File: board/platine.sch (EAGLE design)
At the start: 47 parts, among them IC2 SPS-1, T1 BC846, T2 BC846, X11 22-23-2031, X15 22-23-2031, X16 22-23-2031, X17 22-23-2031, X18 22-23-2031, X3 1751251, X4 1751251, X5 1751251, X7 1751248, X8 1751248, X9 1751248

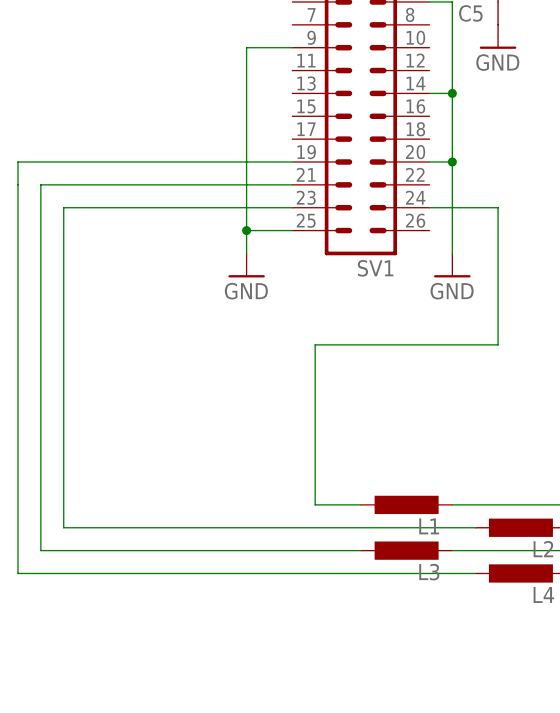
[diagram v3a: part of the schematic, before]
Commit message: fix(board): switch MISO and MOSI
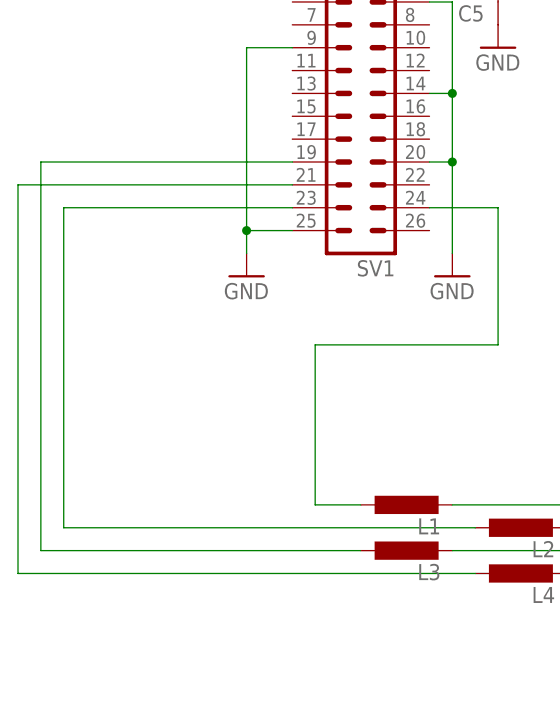
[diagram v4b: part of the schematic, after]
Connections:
- net N$46: now also SV1.19; no longer SV1.21
- net N$6: now also SV1.21; no longer SV1.19
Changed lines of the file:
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@@
 <?xml version="1.0" encoding="utf-8"?>
 <!DOCTYPE eagle SYSTEM "eagle.dtd">
-<eagle version="6.3">
+<eagle version="6.4">
 <drawing>
 <settings>
@@
 <grid distance="0.1" unitdist="inch" unit="inch" style="lines" multiple="1" display="no" altdistance="0.01" altunitdist="inch" altunit="inch"/>
 <layers>
-<layer number="1" name="Top" color="4" fill="1" visible="yes" active="no"/>
-<layer number="2" name="Route2" color="1" fill="3" visible="yes" active="no"/>
-<layer number="3" name="Route3" color="4" fill="3" visible="yes" active="no"/>
-<layer number="4" name="Route4" color="1" fill="4" visible="yes" active="no"/>
-<layer number="5" name="Route5" color="4" fill="4" visible="yes" active="no"/>
-<layer number="6" name="Route6" color="1" fill="8" visible="yes" active="no"/>
-<layer number="7" name="Route7" color="4" fill="8" visible="yes" active="no"/>
-<layer number="8" name="Route8" color="1" fill="2" visible="yes" active="no"/>
-<layer number="9" name="Route9" color="4" fill="2" visible="yes" active="no"/>
-<layer number="10" name="Route10" color="1" fill="7" visible="yes" active="no"/>
-<layer number="11" name="Route11" color="4" fill="7" visible="yes" active="no"/>
-<layer number="12" name="Route12" color="1" fill="5" visible="yes" active="no"/>
-<layer number="13" name="Route13" color="4" fill="5" visible="yes" active="no"/>
-<layer number="14" name="Route14" color="1" fill="6" visible="yes" active="no"/>
-<layer number="15" name="Route15" color="4" fill="6" visible="yes" active="no"/>
-<layer number="16" name="Bottom" color="1" fill="1" visible="yes" active="no"/>
-<layer number="17" name="Pads" color="2" fill="1" visible="yes" active="no"/>
-<layer number="18" name="Vias" color="2" fill="1" visible="yes" active="no"/>
-<layer number="19" name="Unrouted" color="6" fill="1" visible="yes" active="no"/>
-<layer number="20" name="Dimension" color="15" fill="1" visible="yes" active="no"/>
-<layer number="21" name="tPlace" color="7" fill="1" visible="yes" active="no"/>
-<layer number="22" name="bPlace" color="7" fill="1" visible="yes" active="no"/>
-<layer number="23" name="tOrigins" color="15" fill="1" visible="yes" active="no"/>
-<layer number="24" name="bOrigins" color="15" fill="1" visible="yes" active="no"/>
-<layer number="25" name="tNames" color="7" fill="1" visible="yes" active="no"/>
-<layer number="26" name="bNames" color="7" fill="1" visible="yes" active="no"/>
-<layer number="27" name="tValues" color="7" fill="1" visible="yes" active="no"/>
-<layer number="28" name="bValues" color="7" fill="1" visible="yes" active="no"/>
+<layer number="1" name="Top" color="4" fill="1" visible="no" active="no"/>
+<layer number="2" name="Route2" color="1" fill="3" visible="no" active="no"/>
+<layer number="3" name="Route3" color="4" fill="3" visible="no" active="no"/>
+<layer number="4" name="Route4" color="1" fill="4" visible="no" active="no"/>
+<layer number="5" name="Route5" color="4" fill="4" visible="no" active="no"/>
+<layer number="6" name="Route6" color="1" fill="8" visible="no" active="no"/>
+<layer number="7" name="Route7" color="4" fill="8" visible="no" active="no"/>
+<layer number="8" name="Route8" color="1" fill="2" visible="no" active="no"/>
+<layer number="9" name="Route9" color="4" fill="2" visible="no" active="no"/>
+<layer number="10" name="Route10" color="1" fill="7" visible="no" active="no"/>
+<layer number="11" name="Route11" color="4" fill="7" visible="no" active="no"/>
+<layer number="12" name="Route12" color="1" fill="5" visible="no" active="no"/>
+<layer number="13" name="Route13" color="4" fill="5" visible="no" active="no"/>
+<layer number="14" name="Route14" color="1" fill="6" visible="no" active="no"/>
+<layer number="15" name="Route15" color="4" fill="6" visible="no" active="no"/>
+<layer number="16" name="Bottom" color="1" fill="1" visible="no" active="no"/>
+<layer number="17" name="Pads" color="2" fill="1" visible="no" active="no"/>
+<layer number="18" name="Vias" color="2" fill="1" visible="no" active="no"/>
+<layer number="19" name="Unrouted" color="6" fill="1" visible="no" active="no"/>
+<layer number="20" name="Dimension" color="15" fill="1" visible="no" active="no"/>
+<layer number="21" name="tPlace" color="7" fill="1" visible="no" active="no"/>
+<layer number="22" name="bPlace" color="7" fill="1" visible="no" active="no"/>
+<layer number="23" name="tOrigins" color="15" fill="1" visible="no" active="no"/>
+<layer number="24" name="bOrigins" color="15" fill="1" visible="no" active="no"/>
+<layer number="25" name="tNames" color="7" fill="1" visible="no" active="no"/>
+<layer number="26" name="bNames" color="7" fill="1" visible="no" active="no"/>
+<layer number="27" name="tValues" color="7" fill="1" visible="no" active="no"/>
+<layer number="28" name="bValues" color="7" fill="1" visible="no" active="no"/>
 <layer number="29" name="tStop" color="7" fill="3" visible="no" active="no"/>
 <layer number="30" name="bStop" color="7" fill="6" visible="no" active="no"/>
@@
 <layer number="35" name="tGlue" color="7" fill="4" visible="no" active="no"/>
 <layer number="36" name="bGlue" color="7" fill="5" visible="no" active="no"/>
-<layer number="37" name="tTest" color="7" fill="1" visible="yes" active="no"/>
-<layer number="38" name="bTest" color="7" fill="1" visible="yes" active="no"/>
+<layer number="37" name="tTest" color="7" fill="1" visible="no" active="no"/>
+<layer number="38" name="bTest" color="7" fill="1" visible="no" active="no"/>
 <layer number="39" name="tKeepout" color="4" fill="11" visible="no" active="no"/>
 <layer number="40" name="bKeepout" color="1" fill="11" visible="no" active="no"/>
@@
 <layer number="44" name="Drills" color="7" fill="1" visible="no" active="no"/>
 <layer number="45" name="Holes" color="7" fill="1" visible="no" active="no"/>
-<layer number="46" name="Milling" color="3" fill="1" visible="yes" active="no"/>
-<layer number="47" name="Measures" color="7" fill="1" visible="yes" active="no"/>
-<layer number="48" name="Document" color="7" fill="1" visible="yes" active="no"/>
-<layer number="49" name="Reference" color="7" fill="1" visible="yes" active="no"/>
-<layer number="51" name="tDocu" color="7" fill="1" visible="yes" active="no"/>
-<layer number="52" name="bDocu" color="7" fill="1" visible="yes" active="no"/>
+<layer number="46" name="Milling" color="3" fill="1" visible="no" active="no"/>
+<layer number="47" name="Measures" color="7" fill="1" visible="no" active="no"/>
+<layer number="48" name="Document" color="7" fill="1" visible="no" active="no"/>
+<layer number="49" name="Reference" color="7" fill="1" visible="no" active="no"/>
+<layer number="51" name="tDocu" color="7" fill="1" visible="no" active="no"/>
+<layer number="52" name="bDocu" color="7" fill="1" visible="no" active="no"/>
 <layer number="91" name="Nets" color="2" fill="1" visible="yes" active="yes"/>
 <layer number="92" name="Busses" color="1" fill="1" visible="yes" active="yes"/>
@@
 <pinref part="L4" gate="G$1" pin="1"/>
 <wire x1="-12.7" y1="68.58" x2="-63.5" y2="68.58" width="0.1524" layer="91"/>
-<pinref part="SV1" gate="G$1" pin="19"/>
-<wire x1="-33.02" y1="114.3" x2="-63.5" y2="114.3" width="0.1524" layer="91"/>
-<wire x1="-63.5" y1="114.3" x2="-63.5" y2="111.76" width="0.1524" layer="91"/>
+<pinref part="SV1" gate="G$1" pin="21"/>
+<wire x1="-63.5" y1="111.76" x2="-33.02" y2="111.76" width="0.1524" layer="91"/>
 </segment>
 </net>
@@
 <segment>
 <pinref part="L3" gate="G$1" pin="1"/>
-<wire x1="-60.96" y1="111.76" x2="-60.96" y2="71.12" width="0.1524" layer="91"/>
+<wire x1="-60.96" y1="114.3" x2="-60.96" y2="71.12" width="0.1524" layer="91"/>
 <wire x1="-25.4" y1="71.12" x2="-60.96" y2="71.12" width="0.1524" layer="91"/>
-<pinref part="SV1" gate="G$1" pin="21"/>
-<wire x1="-33.02" y1="111.76" x2="-60.96" y2="111.76" width="0.1524" layer="91"/>
-</segment>
-</net>
+<pinref part="SV1" gate="G$1" pin="19"/>
+<wire x1="-60.96" y1="114.3" x2="-33.02" y2="114.3" width="0.1524" layer="91"/>
+</segment>
+</net>

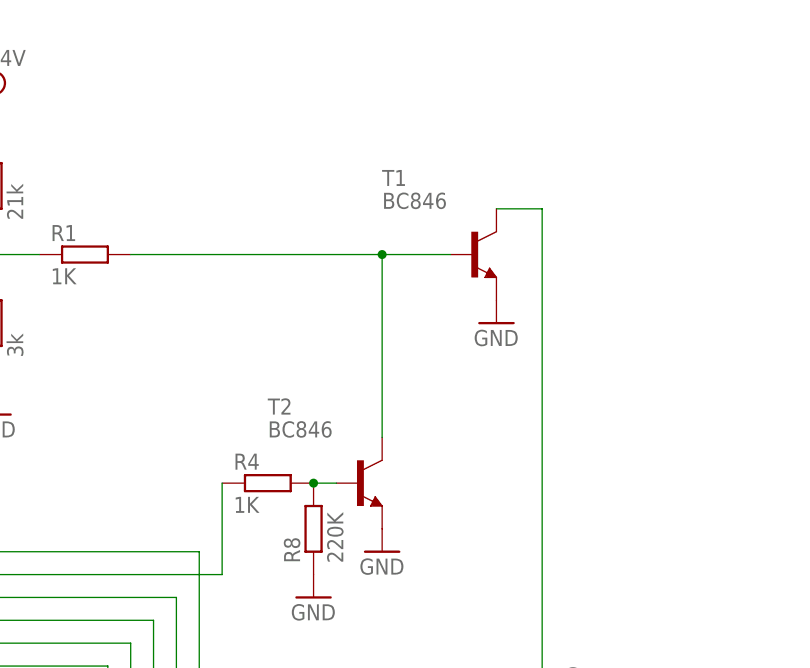
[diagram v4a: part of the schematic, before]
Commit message: Replaced wrong transistor
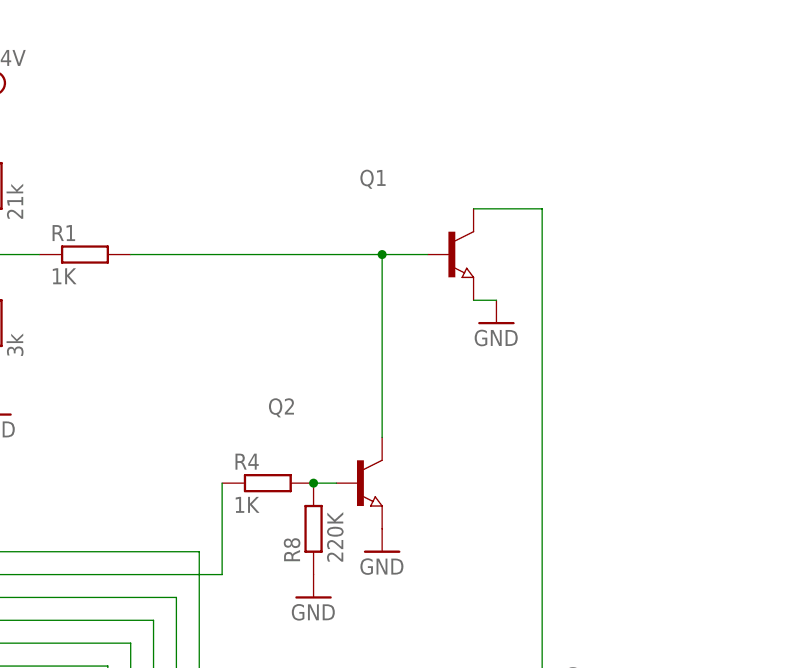
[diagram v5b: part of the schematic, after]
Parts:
- removed T1, T2: BC846, transistor:-NPN-SOT23-EBC
- added Q1, Q2: (no value), semicon-smd-ipc:NPN-TRANSISTOR_SOT23
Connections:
- net GND: now also Q1.E, Q2.E; no longer T1.E, T2.E
- net N$2: now also Q1.B, Q2.C; no longer T1.B, T2.C
- net N$3: now also Q2.B; no longer T2.B
- net N$7: now also Q1.C; no longer T1.C
